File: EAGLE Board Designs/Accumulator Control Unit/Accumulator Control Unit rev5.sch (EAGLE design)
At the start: 243 parts, among them J1 CONNECTOR-12_MF_T_V_, J2 CONNECTOR-6_μF_T_V_BLACK, J3 CONNECTOR-4_μF_T_V_BLACK, J4 CONNECTOR-2_MF_T_V_, J5 CONNECTOR-8_μF_T_V_BLACK, J6 CONNECTOR-14_MF_T_V_, J7 JUMPER__1X02, J8 JUMPER__1X02, K1 RELAY_SOLIDSTATE_NO_CPC1020NTR, Q1 TRANSISTOR_N_MOS__PMV15ENEA, Q2 TRANSISTOR_N_MOS__PMV15ENEA, Q3 TRANSISTOR_N_MOS__PMV15ENEA, Q4 TRANSISTOR_N_MOS__PMV15ENEA, T1 TRANSFORMER_HM2112ZNLT_AIRGAP, U1 VOLTAGE_REGULATOR_SOT-223_3.3V, U10 TCAN1051HQV-Q1, U11 OPAMP_1_CHANNEL_OPA991, U12 OPAMP_1_CHANNEL_OPA991, U13 OPAMP_1_CHANNEL_OPA991, U14 RELAY_SOLIDSTATE_NO_DIP-4, U15 LM555, U16 OPAMP_1_CHANNEL_OPA991, U17 MAX7404, U18 OPAMP_1_CHANNEL_OPA991, U19 MAX7404, U2 RELAY_SOLIDSTATE_NO_DIP-4, U20 LOGICGATE_BUFFER, U21 ADM8316WBX30, U22 OPAMP_1_CHANNEL_OPA991, U23 LOGICGATE_AND_DCK3, U24 LOGICGATE_AND_DCK3, U25 LOGICGATE_AND_DCK3, U26 OPAMP_1_CHANNEL_OPA991, U27 ADG1423, U28 OPAMP_1_CHANNEL_OPA991, U29 MAX7404, U3 RELAY_SOLIDSTATE_NO_DIP-4, U30 OPAMP_1_CHANNEL_OPA991, U31 MAX7404, U4 OPAMP_1_CHANNEL_OPA991, U5 OPAMP_1_CHANNEL_OPA991, U6 TCAN1051HQV-Q1, U7 LTC6820, U8 OPAMP_1_CHANNEL_OPA991, U9 OPAMP_1_CHANNEL_OPA991

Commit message: replace w/ tuned resistor
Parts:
- K1: value RELAY_SOLIDSTATE_NO_CPC1020NTR -> RELAY_SOLIDSTATE_NO_6-SMD; device HyTechDevices:RELAY_SOLIDSTATE_NO_CPC1020NTR -> hytech devices temp:RELAY_SOLIDSTATE_NO_6-SMD
- R45: value RESISTOR_0603_10K -> RESISTOR_0603_3K; device HyTechDevices:RESISTOR_0603_10K -> HyTechDevices:RESISTOR_0603_3K
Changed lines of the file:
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@@
 <part name="P121" library="HyTechSupplies" deviceset="GND" device=""/>
 <part name="P122" library="HyTechSupplies" deviceset="GND" device=""/>
-<part name="K1" library="HyTechDevices" deviceset="RELAY_SOLIDSTATE_NO_*" device="CPC1020NTR"/>
+<part name="K1" library="hytech devices temp" deviceset="RELAY_SOLIDSTATE_NO_*" device="6-SMD"/>
 <part name="U$30" library="HyTechSupplies" deviceset="+24V" device=""/>
 <part name="P11" library="HyTechSupplies" deviceset="GND" device=""/>
-<part name="R45" library="HyTechDevices" deviceset="RESISTOR_?_*" device="0603" technology="10K"/>
+<part name="R45" library="HyTechDevices" deviceset="RESISTOR_?_*" device="0603" technology="3K" value="RESISTOR_0603_3K"/>
 <part name="J3" library="HyTechDevices" deviceset="CONNECTOR-4_?_*" device="μF_T_V" technology="BLACK"/>
 <part name="J1" library="HyTechDevices" deviceset="CONNECTOR-12_?_*" device="MF_T_V"/>

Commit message: removed inverter_en and inverter 24V
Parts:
- removed K1: RELAY_SOLIDSTATE_NO_6-SMD, hytech devices temp:RELAY_SOLIDSTATE_NO_6-SMD
- removed R45: RESISTOR_0603_3K, HyTechDevices:RESISTOR_0603_3K
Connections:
- removed net INVERTER_EN: J6.2, R45.1
- removed net N$38: K1.CONTROL+, R45.2
- net +12V: now also J6.2
- net +24V: no longer K1.CONTACT2
- net GND: no longer K1.CONTROL-
- net INVERTER_24V: no longer K1.CONTACT1
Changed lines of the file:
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@@
 <part name="P121" library="HyTechSupplies" deviceset="GND" device=""/>
 <part name="P122" library="HyTechSupplies" deviceset="GND" device=""/>
-<part name="K1" library="hytech devices temp" deviceset="RELAY_SOLIDSTATE_NO_*" device="6-SMD"/>
-<part name="U$30" library="HyTechSupplies" deviceset="+24V" device=""/>
-<part name="P11" library="HyTechSupplies" deviceset="GND" device=""/>
-<part name="R45" library="HyTechDevices" deviceset="RESISTOR_?_*" device="0603" technology="3K" value="RESISTOR_0603_3K"/>
 <part name="J3" library="HyTechDevices" deviceset="CONNECTOR-4_?_*" device="μF_T_V" technology="BLACK"/>
 <part name="J1" library="HyTechDevices" deviceset="CONNECTOR-12_?_*" device="MF_T_V"/>
@@
 <attribute name="VALUE" x="93.98" y="153.67" size="1.27" layer="96" align="top-center"/>
 </instance>
-<instance part="K1" gate="G$1" x="83.82" y="58.42" smashed="yes">
-<attribute name="NAME" x="83.82" y="59.182" size="1.27" layer="95"/>
-<attribute name="MPN" x="83.82" y="44.958" size="1.27" layer="96" align="top-left"/>
-</instance>
-<instance part="U$30" gate="G$1" x="109.22" y="58.42" smashed="yes">
-<attribute name="VALUE" x="109.22" y="63.5" size="1.778" layer="96" align="bottom-center"/>
-</instance>
-<instance part="P11" gate="1" x="73.66" y="45.72" smashed="yes">
-<attribute name="VALUE" x="73.66" y="44.45" size="1.27" layer="96" align="top-center"/>
-</instance>
-<instance part="R45" gate="G$1" x="76.2" y="55.88" smashed="yes">
-<attribute name="NAME" x="74.93" y="57.15" size="1.27" layer="95" align="bottom-center"/>
-<attribute name="RESISTANCE" x="74.93" y="54.61" size="1.27" layer="96" align="top-center"/>
-</instance>
 <instance part="J3" gate="G$1" x="12.7" y="195.58" smashed="yes">
 <attribute name="MPN" x="12.7" y="182.245" size="1.27" layer="96" align="top-left"/>
@@
 <pinref part="P115" gate="1" pin="GND"/>
 <wire x1="68.58" y1="157.48" x2="93.98" y2="157.48" width="0.1524" layer="91"/>
-</segment>
-<segment>
-<pinref part="K1" gate="G$1" pin="CONTROL-"/>
-<wire x1="81.28" y1="48.26" x2="73.66" y2="48.26" width="0.1524" layer="91"/>
-<pinref part="P11" gate="1" pin="GND"/>
 </segment>
 </net>
@@
 <junction x="132.08" y="157.48"/>
 </segment>
+<segment>
+<pinref part="J6" gate="G$1" pin="2"/>
+<wire x1="68.58" y1="182.88" x2="83.82" y2="182.88" width="0.1524" layer="91"/>
+<label x="83.82" y="182.88" size="1.27" layer="95" xref="yes"/>
+</segment>
 </net>
 <net name="BSPD_CURRENT" class="0">
@@
 <wire x1="218.44" y1="200.66" x2="218.44" y2="195.58" width="0.1524" layer="91"/>
 </segment>
-<segment>
-<pinref part="U$30" gate="G$1" pin="+24V"/>
-<pinref part="K1" gate="G$1" pin="CONTACT2"/>
-<wire x1="109.22" y1="55.88" x2="104.14" y2="55.88" width="0.1524" layer="91"/>
-</segment>
 </net>
 <net name="N$32" class="0">
@@
 </segment>
 </net>
-<net name="INVERTER_EN" class="0">
-<segment>
-<pinref part="J6" gate="G$1" pin="2"/>
-<wire x1="68.58" y1="182.88" x2="83.82" y2="182.88" width="0.1524" layer="91"/>
-<label x="83.82" y="182.88" size="1.27" layer="95" xref="yes"/>
-</segment>
-<segment>
-<wire x1="68.58" y1="55.88" x2="71.12" y2="55.88" width="0.1524" layer="91"/>
-<label x="68.58" y="55.88" size="1.27" layer="95" rot="R180" xref="yes"/>
-<pinref part="R45" gate="G$1" pin="1"/>
-</segment>
-</net>
 <net name="INVERTER_24V" class="0">
-<segment>
-<pinref part="K1" gate="G$1" pin="CONTACT1"/>
-<wire x1="104.14" y1="48.26" x2="109.22" y2="48.26" width="0.1524" layer="91"/>
-<label x="109.22" y="48.26" size="1.27" layer="95" xref="yes"/>
-</segment>
 <segment>
 <pinref part="J1" gate="G$1" pin="1"/>
@@
 </segment>
 </net>
-<net name="N$38" class="0">
-<segment>
-<pinref part="K1" gate="G$1" pin="CONTROL+"/>
-<wire x1="81.28" y1="55.88" x2="78.74" y2="55.88" width="0.1524" layer="91"/>
-<pinref part="R45" gate="G$1" pin="2"/>
-</segment>
-</net>

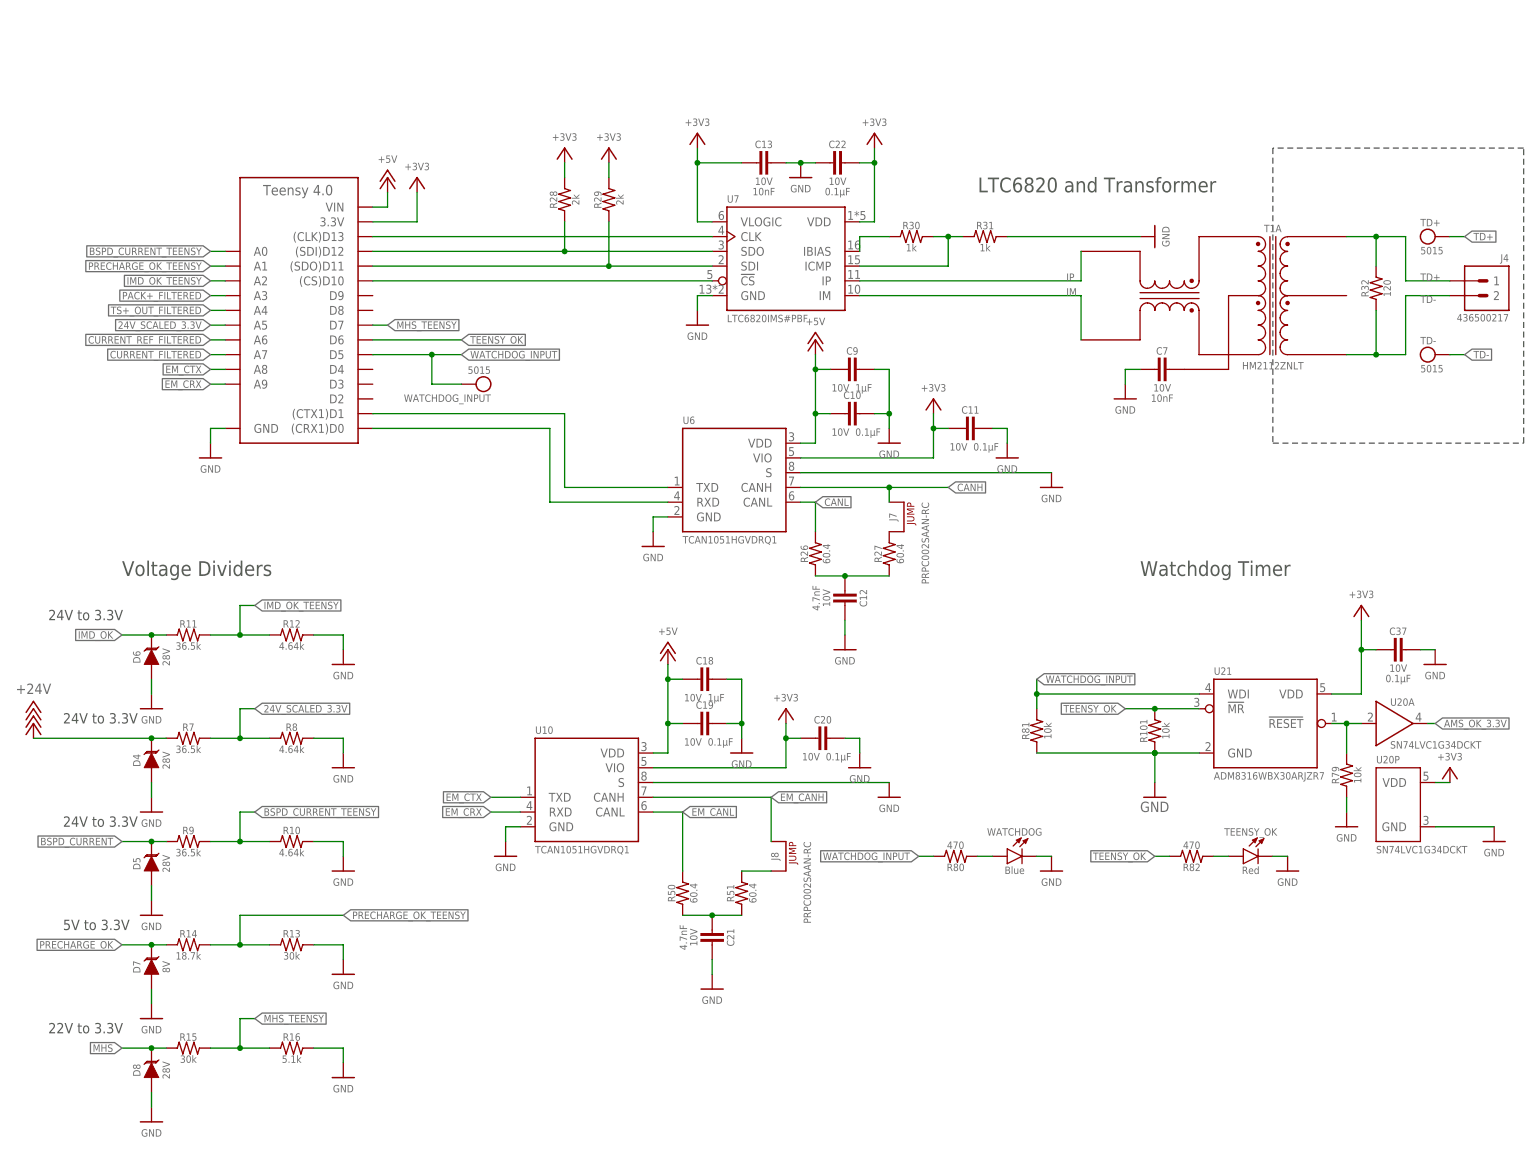
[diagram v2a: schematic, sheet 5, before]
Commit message: begin second isoSPI line
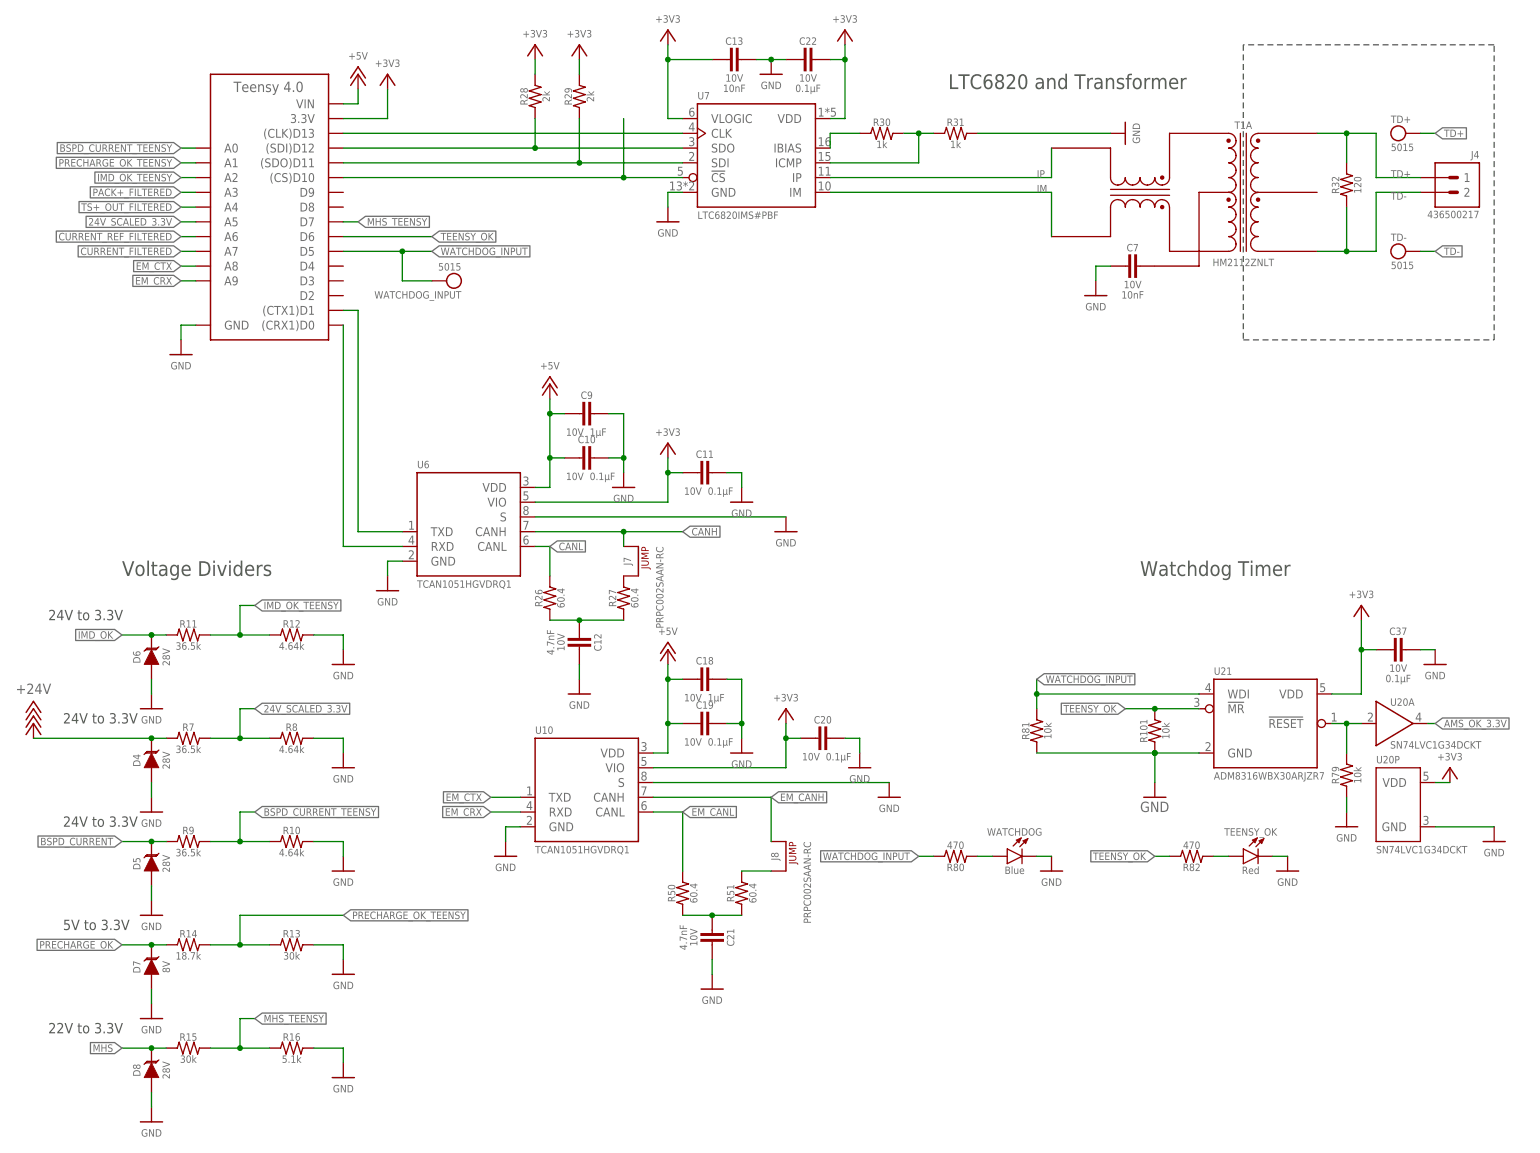
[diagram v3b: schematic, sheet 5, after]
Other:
- moved on the sheet: C10, C11, C12, C13, C22, C7, C9, J4, J7, R26, R27, R28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

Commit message: second 6820 on schematic
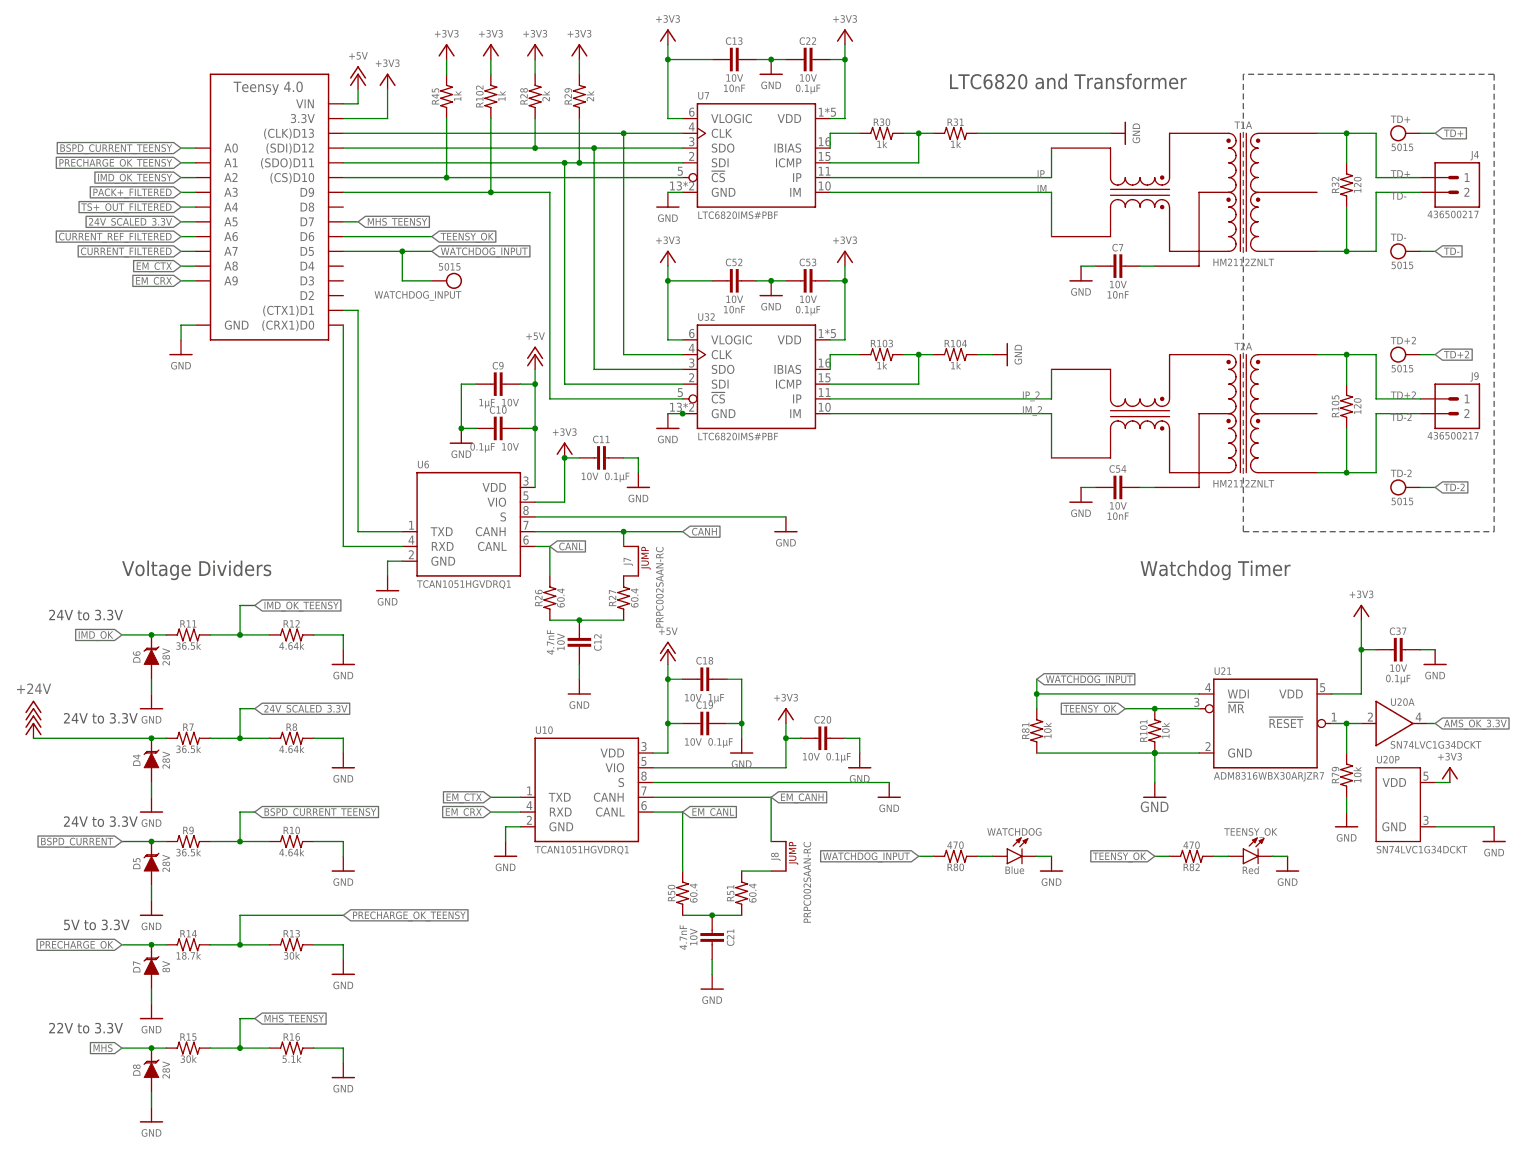
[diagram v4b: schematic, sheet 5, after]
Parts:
- added C52: CAPACITOR_0603_10V_10NF, HyTechDevices:CAPACITOR_0603_10V_10NF
- added C53: CAPACITOR_0603_10V_0.1UF, HyTechDevices:CAPACITOR_0603_10V_0.1UF
- added C54: CAPACITOR_0603_10V_10NF, HyTechDevices - Copy:CAPACITOR_0603_10V_10NF
- added J9: CONNECTOR-2_MF_T_V_, HyTechDevices - Copy:CONNECTOR-2_MF_T_V_
- added R102, R45: RESISTOR_0603_1K, HyTechDevices:RESISTOR_0603_1K
- added R103, R104: RESISTOR_0603_1K, HyTechDevices - Copy:RESISTOR_0603_1K
- added R105: RESISTOR_0603_120, HyTechDevices:RESISTOR_0603_120
- added T2: TRANSFORMER_HM2112ZNLT_AIRGAP, HyTechDevices:TRANSFORMER_HM2112ZNLT_AIRGAP
- added TD+2, TD-2: TEST_POINT, HyTechDevices - Copy:TEST_POINT
- added U32: LTC6820, HyTechDevices:LTC6820
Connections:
- new net IM_2: T2A.TD-, U32.IM
- new net IP_2: T2A.TD+, U32.IP
- new net N$38: R103.1, U32.IBIAS
- new net N$40: A3.D9, R102.1, U32.!CS
- new net N$42: R103.2, R104.1, U32.ICMP
- new net N$62: C54.1, T2A.TCT
- new net TD+2: J9.1, R105.2, T2A.MX+, TD+2.P$1
- new net TD-2: J9.2, R105.1, T2A.MX-, TD-2.P$1
- net +3V3: now also C52.2, C53.1, R102.2, R45.2, U32.VDD, U32.VLOGIC
- net CS_LTC_6820: now also R45.1
- net GND: now also C52.1, C53.2, C54.2, R104.2, U32.GND
- net N$13: now also U32.SDI
- net N$43: now also U32.SDO
- net N$44: now also U32.CLK
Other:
- moved on the sheet: C10, C11, C7, C9
